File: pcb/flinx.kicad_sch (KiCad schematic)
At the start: 139 parts, among them J1 USB_C_Receptacle_USB2.0_14P, SW1 SW_Push, SW10 SW_Push, SW11 SW_Push, SW12 SW_Push, SW13 SW_Push, SW14 SW_Push, SW15 SW_Push, SW16 SW_Push, SW17 SW_Push, SW18 SW_Push, SW19 SW_Push, SW2 SW_Push, SW20 SW_Push, SW21 SW_Push, SW22 SW_Push, SW23 SW_Push, SW24 SW_Push, SW25 SW_Push, SW26 SW_Push, SW27 SW_Push, SW28 SW_Push, SW29 SW_Push, SW3 SW_Push, SW30 SW_Push, SW31 SW_Push, SW32 SW_Push, SW33 SW_Push, SW34 SW_Push, SW35 SW_Push, SW36 SW_Push, SW37 SW_Push, SW38 SW_Push, SW39 SW_Push, SW4 SW_Push, SW40 SW_Push, SW41 SW_Push, SW42 SW_Push, SW43 SW_Push, SW44 SW_Push, SW45 SW_Push, SW46 SW_Push, SW47 SW_Push, SW48 SW_Push, SW49 SW_SPDT, SW5 SW_Push, SW6 SW_Push, SW7 SW_Push, SW8 SW_Push, SW9 SW_Push, U1 nRF52833_QDxx, U2 TP4057, Y1 32MHz

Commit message: Update PCB
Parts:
- removed Y1: 32MHz, Crystal:Crystal_SMD_MicroCrystal_CC7V-T1A-2Pin_3.2x1.5mm, symbol Device:Crystal
- added Y1: 32MHz, Crystal:Crystal_SMD_SeikoEpson_FA128-4Pin_2.0x1.6mm, symbol Device:Crystal_GND24
- L1, L3, L4: value 4.7nH -> 4.7 nH
- L2: value 2.2nH -> 2.2 nH
- L5: value 2.7nH -> 2.7 nH
- L6: value 3.3nH -> 3.3 nH
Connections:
- net GND: now also Y1.2 (G), Y1.4 (G)
- net at C1.1, U1.28 (XC1): now also Y1.1
- net at C2.1, U1.29 (XC2): now also Y1.3
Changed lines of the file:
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@@
 	)
 	(junction
-		(at 130.81 87.63)
+		(at 31.75 78.74)
 		(diameter 0)
 		(color 0 0 0 0)
 	)
 	(junction
-		(at 31.75 78.74)
+		(at 123.19 87.63)
 		(diameter 0)
 		(color 0 0 0 0)
@@
 	)
 	(junction
+		(at 130.81 87.63)
+		(diameter 0)
+		(color 0 0 0 0)
+	)
+	(junction
 		(at 207.01 163.83)
 		(diameter 0)
@@
 	)
 	(junction
-		(at 123.19 87.63)
-		(diameter 0)
-		(color 0 0 0 0)
-	)
-	(junction
 		(at 69.85 163.83)
 		(diameter 0)
@@
 	(wire
 		(pts
+			(xy 127 92.71) (xy 127 95.25)
+		)
+		(stroke
+			(width 0)
+			(type default)
+		)
+	)
+	(wire
+		(pts
 			(xy 38.1 43.18) (xy 38.1 48.26)
 		)
@@
 			)
 		)
-		(property "Value" "4.7nH"
+		(property "Value" "4.7 nH"
 			(at 43.18 40.64 90)
 			(show_name no)
@@
 			)
 		)
-		(property "Value" "4.7nH"
+		(property "Value" "4.7 nH"
 			(at 85.09 85.09 90)
 			(show_name no)
@@
 			)
 		)
-		(property "Value" "2.7nH"
+		(property "Value" "2.7 nH"
 			(at 102.87 105.4099 0)
 			(show_name no)
@@
 			)
 		)
-		(property "Value" "4.7nH"
+		(property "Value" "4.7 nH"
 			(at 52.07 40.64 90)
 			(show_name no)
@@
 			)
 		)
-		(property "Value" "3.3nH"
+		(property "Value" "3.3 nH"
 			(at 106.68 97.79 90)
 			(show_name no)
@@
 			)
 		)
-		(property "Value" "2.2nH"
+		(property "Value" "2.2 nH"
 			(at 92.71 85.09 90)
 			(show_name no)
@@
 	)
 	(symbol
+		(lib_id "Device:Crystal_GND24")
+		(at 127 87.63 0)
+		(unit 1)
+		(body_style 1)
+		(exclude_from_sim no)
+		(in_bom yes)
+		(on_board yes)
+		(in_pos_files yes)
+		(dnp no)
+		(fields_autoplaced yes)
+		(property "Reference" "Y1"
+			(at 127 78.74 0)
+			(show_name no)
+			(do_not_autoplace no)
+			(effects
+				(font
+					(size 1.27 1.27)
+				)
+			)
+		)
+		(property "Value" "32MHz"
+			(at 127 81.28 0)
+			(show_name no)
+			(do_not_autoplace no)
+			(effects
+				(font
+					(size 1.27 1.27)
+				)
+			)
+		)
+		(property "Footprint" "Crystal:Crystal_SMD_SeikoEpson_FA128-4Pin_2.0x1.6mm"
+			(at 127 87.63 0)
+			(hide yes)
+			(show_name no)
+			(do_not_autoplace no)
+			(effects
+				(font
+					(size 1.27 1.27)
+				)
+			)
+		)
+		(property "Datasheet" ""
+			(at 127 87.63 0)
+			(hide yes)
+			(show_name no)
+			(do_not_autoplace no)
+			(effects
+				(font
+					(size 1.27 1.27)
+				)
+			)
+		)
+		(property "Description" "Four pin crystal, GND on pins 2 and 4"
+			(at 127 87.63 0)
+			(hide yes)
+			(show_name no)
+			(do_not_autoplace no)
+			(effects
+				(font
+					(size 1.27 1.27)
+				)
+			)
+		)
+		(property private "KLC_S3.3" "The rectangle is not a symbol body but a graphical element"
+			(at 127 100.33 0)
+			(hide yes)
+			(show_name yes)
+			(do_not_autoplace no)
+			(effects
+				(font
+					(size 1.27 1.27)
+				)
+			)
+		)
+		(property private "KLC_S4.1" "Some pins are on 50mil grid to make the symbol small"
+			(at 127 102.87 0)
+			(hide yes)
+			(show_name yes)
+			(do_not_autoplace no)
+			(effects
+				(font
+					(size 1.27 1.27)
+				)
+			)
+		)
+		(pin "3"
+		)
+		(pin "4"
+		)
+		(pin "1"
+		)
+		(pin "2"
+		)
+		(instances
+			(project "flinx"
+				(path "/cb115450-b63d-4583-9c68-cd7130599f33"
+					(reference "Y1")
+					(unit 1)
+				)
+			)
+		)
+	)
+	(symbol
 		(lib_id "Device:R")
 		(at 267.97 104.14 0)
@@
 					(unit 1)
 				)
-			)
-		)
-	)
-	(symbol
-		(lib_id "Device:Crystal")
-		(at 127 87.63 0)
-		(unit 1)
-		(body_style 1)
-		(exclude_from_sim no)
-		(in_bom yes)
-		(on_board yes)
-		(in_pos_files yes)
-		(dnp no)
-		(fields_autoplaced yes)
-		(property "Reference" "Y1"
-			(at 127 80.01 0)
-			(show_name no)
-			(do_not_autoplace no)
-			(effects
-				(font
-					(size 1.27 1.27)
-				)
-			)
-		)
-		(property "Value" "32MHz"
-			(at 127 82.55 0)
-			(show_name no)
-			(do_not_autoplace no)
-			(effects
-				(font
-					(size 1.27 1.27)
-				)
-			)
-		)
-		(property "Footprint" "Crystal:Crystal_SMD_MicroCrystal_CC7V-T1A-2Pin_3.2x1.5mm"
-			(at 127 87.63 0)
-			(hide yes)
-			(show_name no)
-			(do_not_autoplace no)
-			(effects
-				(font
-					(size 1.27 1.27)
-				)
-			)
-		)
-		(property "Datasheet" ""
-			(at 127 87.63 0)
-			(hide yes)
-			(show_name no)
-			(do_not_autoplace no)
-			(effects
-				(font
-					(size 1.27 1.27)
-				)
-			)
-		)
-		(property "Description" "Two pin crystal"
-			(at 127 87.63 0)
-			(hide yes)
-			(show_name no)
-			(do_not_autoplace no)
-			(effects
-				(font
-					(size 1.27 1.27)
-				)
-			)
-		)
-		(pin "1"
-		)
-		(pin "2"
-		)
-		(instances
-			(project "flinx"
-				(path "/cb115450-b63d-4583-9c68-cd7130599f33"
-					(reference "Y1")
-					(unit 1)
-				)

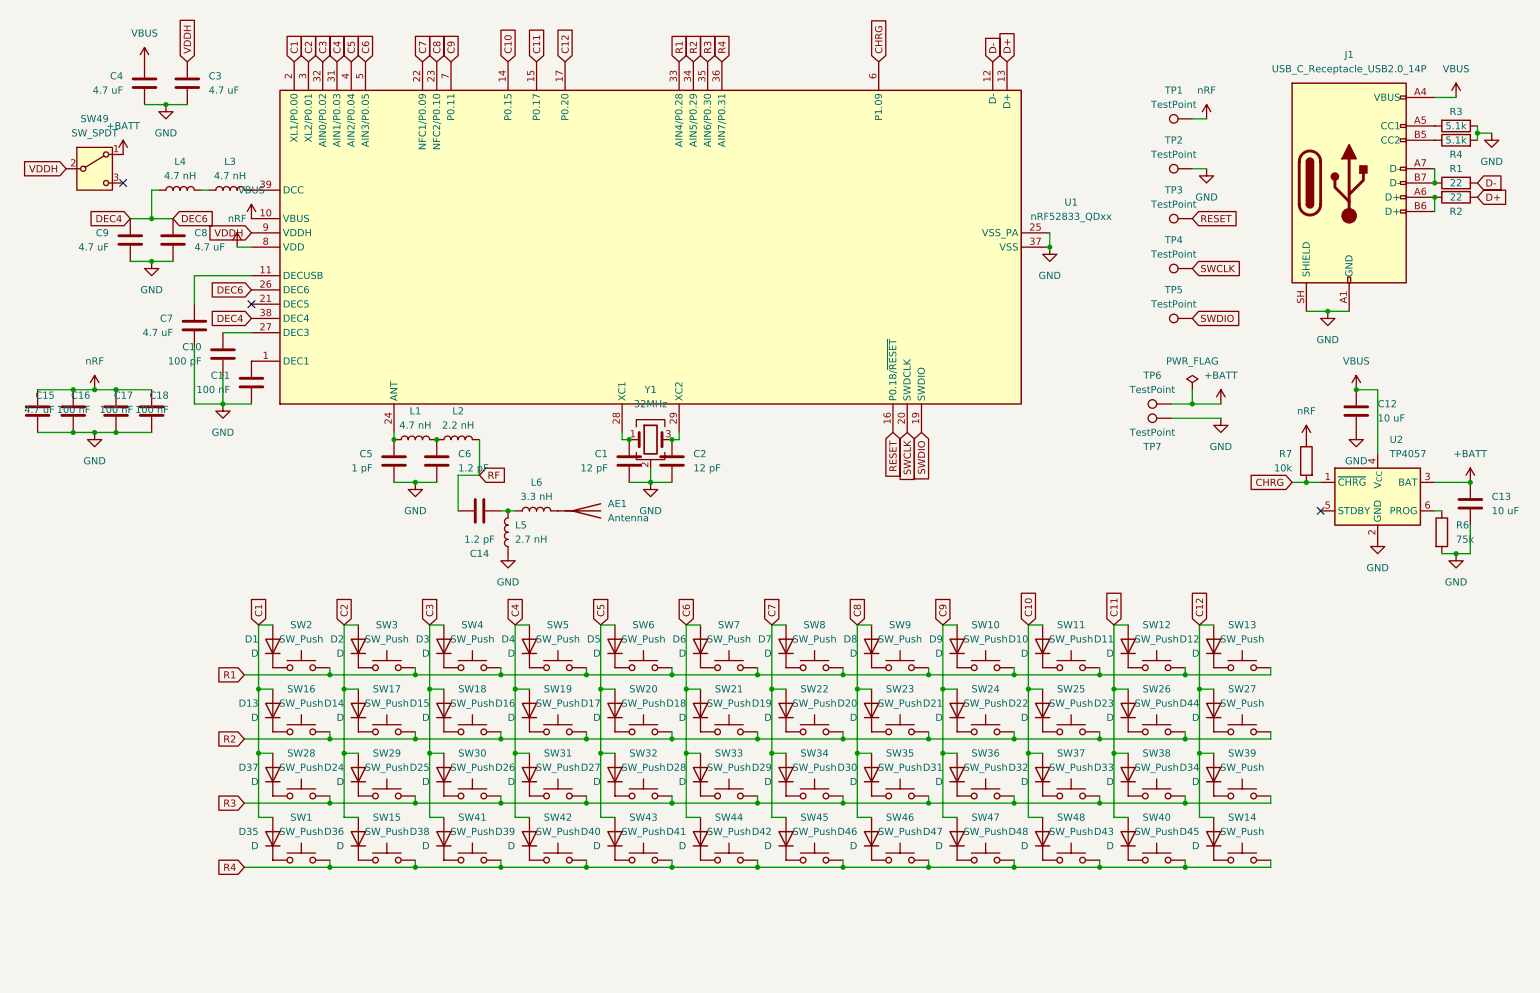
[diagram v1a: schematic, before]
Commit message: Swap to BL654
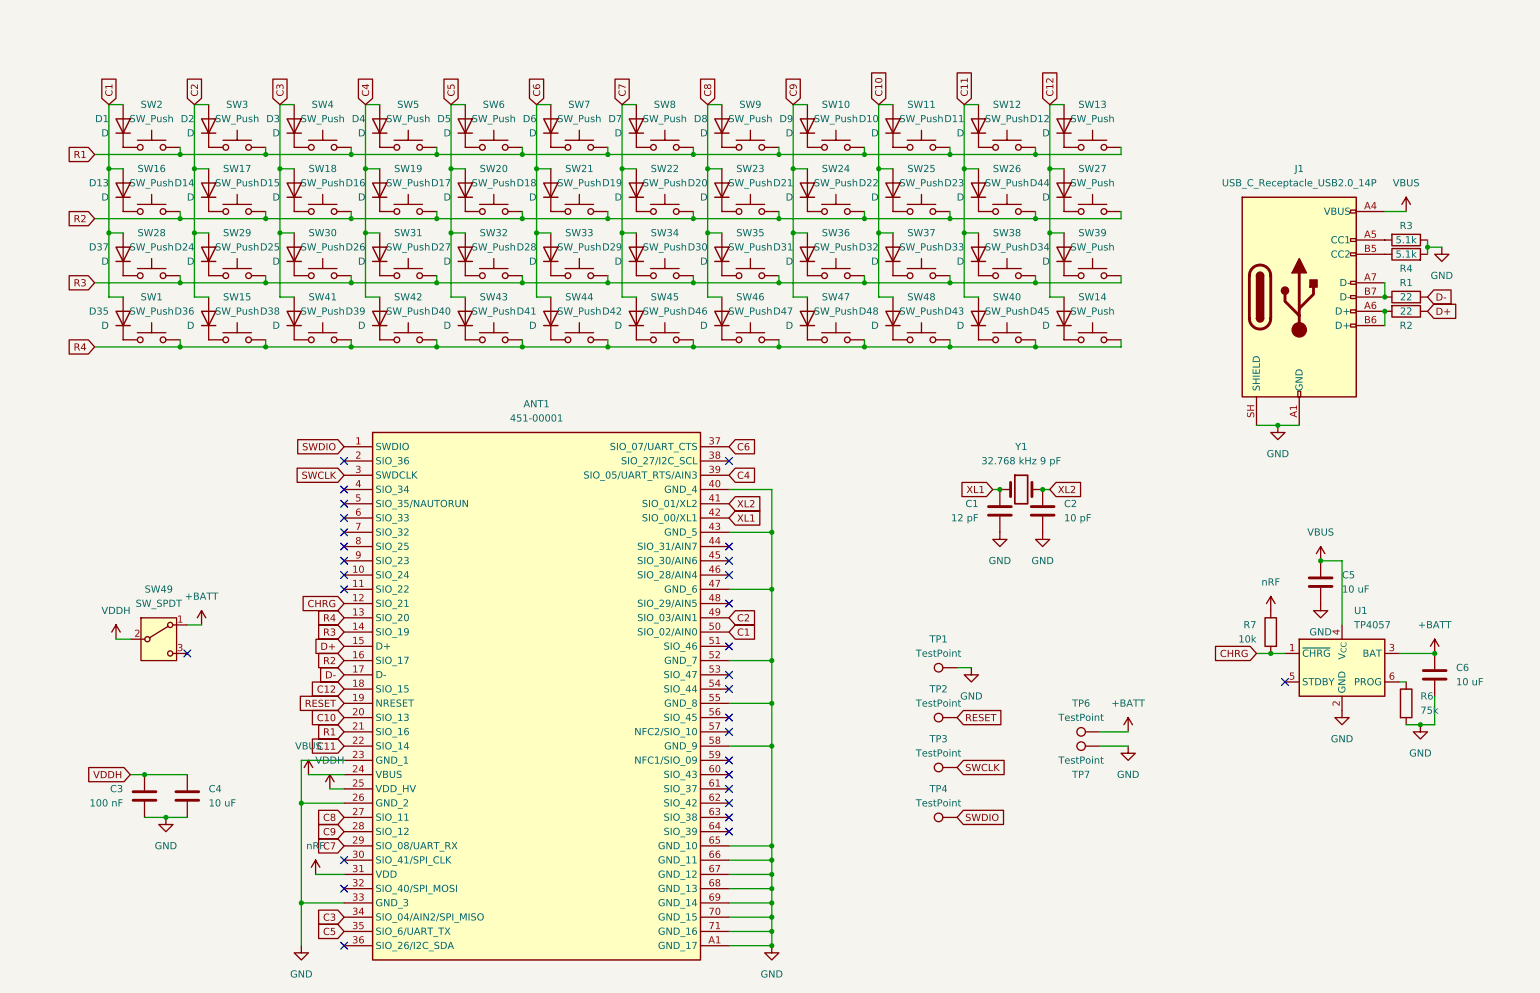
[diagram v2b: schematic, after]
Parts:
- removed AE1: Antenna, RF_Antenna:Johanson_2450AT18x100, symbol Device:Antenna
- removed C10: 100 pF, Capacitor_SMD:C_0603_1608Metric, symbol Device:C
- removed C11, C16, C17, C18: 100 nF, Capacitor_SMD:C_0603_1608Metric, symbol Device:C
- removed C14, C6: 1.2 pF, Capacitor_SMD:C_0603_1608Metric, symbol Device:C
- removed C15, C7, C8, C9: 4.7 uF, Capacitor_SMD:C_0603_1608Metric, symbol Device:C
- removed C5: 1 pF, Capacitor_SMD:C_0603_1608Metric, symbol Device:C
- removed L1, L3, L4: 4.7 nH, Inductor_SMD:L_0603_1608Metric, symbol Device:L
- removed L2: 2.2 nH, Inductor_SMD:L_0603_1608Metric, symbol Device:L
- removed L5: 2.7 nH, Inductor_SMD:L_0603_1608Metric, symbol Device:L
- removed L6: 3.3 nH, Inductor_SMD:L_0603_1608Metric, symbol Device:L
- removed TP5: TestPoint, Project:Pad_SMD_1.5x1.5, symbol Connector:TestPoint
- removed U1: nRF52833_QDxx, Package_DFN_QFN:QFN-40-1EP_5x5mm_P0.4mm_EP3.6x3.6mm, symbol MCU_Nordic:nRF52833_QDxx
- removed Y1: 32MHz, Crystal:Crystal_SMD_SeikoEpson_FA128-4Pin_2.0x1.6mm, symbol Device:Crystal_GND24
- added ANT1: 451-00001, Project:45100001, symbol Project:451-00001
- added Y1: 32.768 kHz 9 pF, Crystal:Crystal_SMD_MicroCrystal_CC7V-T1A-2Pin_3.2x1.5mm_HandSoldering, symbol Device:Crystal
- C2: value 12 pF -> 10 pF
- C3: value 4.7 uF -> 100 nF
- C4: value 4.7 uF -> 10 uF
- renumbered C12 to C5, C13 to C6, U2 to U1
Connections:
- net C1: now also ANT1.50 (SIO_02/AIN0)
- net C10: now also ANT1.20 (SIO_13)
- net C11: now also ANT1.22 (SIO_14)
- net C12: now also ANT1.18 (SIO_15)
- net C2: now also ANT1.49 (SIO_03/AIN1)
- net C3: now also ANT1.34 (SIO_04/AIN2/SPI_MISO)
- net C4: now also ANT1.39 (SIO_05/UART_RTS/AIN3)
- net C5: now also ANT1.35 (SIO_6/UART_TX)
- net C6: now also ANT1.37 (SIO_07/UART_CTS)
- net C7: now also ANT1.29 (SIO_08/UART_RX)
- net C8: now also ANT1.27 (SIO_11)
- net C9: now also ANT1.28 (SIO_12)
- net CHRG: now also ANT1.12 (SIO_21)
- net D+: now also ANT1.15 (D+)
- net D-: now also ANT1.17 (D-)
- net GND: now also TP1.1, ANT1.23 (GND_1), ANT1.26 (GND_2), ANT1.33 (GND_3), ANT1.40 (GND_4), ANT1.43 (GND_5), ANT1.47 (GND_6), ANT1.52 (GND_7), ANT1.55 (GND_8), ANT1.58 (GND_9), ANT1.65 (GND_10), ANT1.66 (GND_11), ANT1.67 (GND_12), ANT1.68 (GND_13), ANT1.69 (GND_14), ANT1.70 (GND_15), ANT1.71 (GND_16), ANT1.A1 (GND_17); no longer TP2.1
- net R1: now also ANT1.21 (SIO_16)
- net R2: now also ANT1.16 (SIO_17)
- net R3: now also ANT1.14 (SIO_19)
- net R4: now also ANT1.13 (SIO_20)
- net RESET: now also TP2.1, ANT1.19 (NRESET); no longer TP3.1
- net SWCLK: now also TP3.1, ANT1.3 (SWDCLK); no longer TP4.1
- net SWDIO: now also TP4.1, ANT1.1 (SWDIO)
- net VBUS: now also ANT1.24 (VBUS); no longer C4.1
- net VDDH: now also C4.1, ANT1.25 (VDD_HV)
- net nRF: now also ANT1.31 (VDD); no longer TP1.1
- net XL1: now reaches C1.1
- net XL1: now also ANT1.42 (SIO_00/XL1), Y1.1
- net XL2: now reaches C2.1
- net XL2: now also ANT1.41 (SIO_01/XL2), Y1.2
- no-connect marks 3 -> 30
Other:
- moved on the sheet: C5, C6, D1, D10, D11, D12, D13, D14, D15, D16, D17, D18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

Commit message: Move decoupling caps
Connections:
- net GND: now also C3.1, C4.1; no longer C3.2, C4.2
- net VDDH: now also C3.2, C4.2; no longer C3.1, C4.1
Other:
- moved on the sheet: C4
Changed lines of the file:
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@@
 	)
 	(junction
-		(at 148.59 114.3)
+		(at 36.83 147.32)
 		(diameter 0)
 		(color 0 0 0 0)
 	)
 	(junction
-		(at 195.58 36.83)
+		(at 148.59 114.3)
 		(diameter 0)
 		(color 0 0 0 0)
 	)
 	(junction
-		(at 119.38 48.26)
+		(at 195.58 36.83)
 		(diameter 0)
 		(color 0 0 0 0)
 	)
 	(junction
-		(at 36.83 147.32)
+		(at 119.38 48.26)
 		(diameter 0)
 		(color 0 0 0 0)
@@
 	(wire
 		(pts
-			(xy 34.29 147.32) (xy 36.83 147.32)
-		)
-		(stroke
-			(width 0)
-			(type default)
-		)
-	)
-	(wire
-		(pts
 			(xy 265.43 53.34) (xy 267.97 53.34)
 		)
@@
 	(wire
 		(pts
+			(xy 36.83 147.32) (xy 44.45 147.32)
+		)
+		(stroke
+			(width 0)
+			(type default)
+		)
+	)
+	(wire
+		(pts
 			(xy 58.42 36.83) (xy 73.66 36.83)
 		)
@@
 	(wire
 		(pts
-			(xy 36.83 147.32) (xy 44.45 147.32)
+			(xy 58.42 59.69) (xy 73.66 59.69)
 		)
 		(stroke
@@
 	(wire
 		(pts
-			(xy 58.42 59.69) (xy 73.66 59.69)
+			(xy 60.96 50.8) (xy 60.96 62.23)
 		)
 		(stroke
@@
 	(wire
 		(pts
-			(xy 60.96 50.8) (xy 60.96 62.23)
+			(xy 88.9 71.12) (xy 88.9 69.85)
 		)
 		(stroke
@@
 	(wire
 		(pts
-			(xy 88.9 71.12) (xy 88.9 69.85)
+			(xy 187.96 96.52) (xy 189.23 96.52)
 		)
 		(stroke
@@
 	(wire
 		(pts
-			(xy 187.96 96.52) (xy 189.23 96.52)
+			(xy 34.29 147.32) (xy 36.83 147.32)
 		)
 		(stroke
@@
 	(symbol
 		(lib_id "Device:C")
-		(at 44.45 151.13 0)
+		(at 44.45 151.13 180)
 		(unit 1)
 		(body_style 1)
@@
 					(size 1.27 1.27)
 				)
-				(justify left)
+				(justify right)
 			)
 		)
@@
 					(size 1.27 1.27)
 				)
-				(justify left)
+				(justify right)
 			)
 		)
 		(property "Footprint" "Capacitor_SMD:C_0603_1608Metric"
-			(at 45.4152 154.94 0)
+			(at 43.4848 147.32 0)
 			(hide yes)
 			(show_name no)
@@
 	)
 	(symbol
-		(lib_id "Device:C")
-		(at 36.83 151.13 0)
-		(mirror y)
-		(unit 1)
-		(body_style 1)
-		(exclude_from_sim no)
-		(in_bom yes)
-		(on_board yes)
-		(in_pos_files yes)
-		(dnp no)
-		(property "Reference" "C3"
-			(at 33.02 149.8599 0)
-			(show_name no)
-			(do_not_autoplace no)
-			(effects
-				(font
-					(size 1.27 1.27)
-				)
-				(justify left)
-			)
-		)
-		(property "Value" "100 nF"
-			(at 33.02 152.3999 0)
-			(show_name no)
-			(do_not_autoplace no)
-			(effects
-				(font
-					(size 1.27 1.27)
-				)
-				(justify left)
-			)
-		)
-		(property "Footprint" "Capacitor_SMD:C_0603_1608Metric"
-			(at 35.8648 154.94 0)
-			(hide yes)
-			(show_name no)
-			(do_not_autoplace no)
-			(effects
-				(font
-					(size 1.27 1.27)
-				)
-			)
-		)
-		(property "Datasheet" ""
-			(at 36.83 151.13 0)
-			(hide yes)
-			(show_name no)
-			(do_not_autoplace no)
-			(effects
-				(font
-					(size 1.27 1.27)
-				)
-			)
-		)
-		(property "Description" "Unpolarized capacitor"
-			(at 36.83 151.13 0)
-			(hide yes)
-			(show_name no)
-			(do_not_autoplace no)
-			(effects
-				(font
-					(size 1.27 1.27)
-				)
-			)
-		)
-		(pin "1"
-		)
-		(pin "2"
-		)
-		(instances
-			(project "flinx"
-				(path "/cb115450-b63d-4583-9c68-cd7130599f33"
-					(reference "C3")
-					(unit 1)
-				)
-			)
-		)
-	)
-	(symbol
 		(lib_id "Device:D")
 		(at 124.46 54.61 270)
@@
 					(unit 1)
 				)
+			)
+		)
+	)
+	(symbol
+		(lib_id "Device:C")
+		(at 36.83 151.13 0)
+		(mirror x)
+		(unit 1)
+		(body_style 1)
+		(exclude_from_sim no)
+		(in_bom yes)
+		(on_board yes)
+		(in_pos_files yes)
+		(dnp no)
+		(property "Reference" "C3"
+			(at 33.02 149.8599 0)
+			(show_name no)
+			(do_not_autoplace no)
+			(effects
+				(font
+					(size 1.27 1.27)
+				)
+				(justify right)
+			)
+		)
+		(property "Value" "100 nF"
+			(at 33.02 152.3999 0)
+			(show_name no)
+			(do_not_autoplace no)
+			(effects
+				(font
+					(size 1.27 1.27)
+				)
+				(justify right)
+			)
+		)
+		(property "Footprint" "Capacitor_SMD:C_0603_1608Metric"
+			(at 37.7952 147.32 0)
+			(hide yes)
+			(show_name no)
+			(do_not_autoplace no)
+			(effects
+				(font
+					(size 1.27 1.27)
+				)
+			)
+		)
+		(property "Datasheet" ""
+			(at 36.83 151.13 0)
+			(hide yes)
+			(show_name no)
+			(do_not_autoplace no)
+			(effects
+				(font
+					(size 1.27 1.27)
+				)
+			)
+		)
+		(property "Description" "Unpolarized capacitor"
+			(at 36.83 151.13 0)
+			(hide yes)
+			(show_name no)
+			(do_not_autoplace no)
+			(effects
+				(font
+					(size 1.27 1.27)
+				)
+			)
+		)
+		(pin "1"
+		)
+		(pin "2"
+		)
+		(instances
+			(project "flinx"
+				(path "/cb115450-b63d-4583-9c68-cd7130599f33"
+					(reference "C3")
+					(unit 1)
+				)

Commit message: Update value
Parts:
- R6: value 75k -> 10k
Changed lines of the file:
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@@
 	)
 	(junction
-		(at 119.38 71.12)
+		(at 40.64 147.32)
 		(diameter 0)
 		(color 0 0 0 0)
 	)
 	(junction
-		(at 36.83 147.32)
+		(at 119.38 71.12)
 		(diameter 0)
 		(color 0 0 0 0)
@@
 	(wire
 		(pts
+			(xy 40.64 147.32) (xy 44.45 147.32)
+		)
+		(stroke
+			(width 0)
+			(type default)
+		)
+	)
+	(wire
+		(pts
 			(xy 237.49 125.73) (xy 240.03 125.73)
 		)
@@
 	(wire
 		(pts
-			(xy 36.83 147.32) (xy 44.45 147.32)
+			(xy 36.83 147.32) (xy 40.64 147.32)
 		)
 		(stroke
@@
 	(wire
 		(pts
-			(xy 34.29 147.32) (xy 36.83 147.32)
-		)
-		(stroke
-			(width 0)
-			(type default)
-		)
-	)
-	(wire
-		(pts
 			(xy 210.82 71.12) (xy 210.82 69.85)
 		)
@@
 		)
 	)
-	(global_label "VDDH"
-		(shape input)
-		(at 34.29 147.32 180)
-		(fields_autoplaced yes)
-		(effects
-			(font
-				(size 1.27 1.27)
-			)
-			(justify right)
-		)
-		(property "Intersheetrefs" "${INTERSHEET_REFS}"
-			(at 26.3457 147.32 0)
-			(hide yes)
-			(show_name no)
-			(do_not_autoplace no)
-			(effects
-				(font
-					(size 1.27 1.27)
-				)
-				(justify right)
-			)
-		)
-	)
 	(global_label "R1"
 		(shape input)
@@
 			)
 		)
-		(property "Value" "75k"
+		(property "Value" "10k"
 			(at 264.16 135.8899 0)
 			(show_name no)
@@
 					(unit 1)
 				)
+			)
+		)
+	)
+	(symbol
+		(lib_id "power:+BATT")
+		(at 40.64 147.32 0)
+		(unit 1)
+		(body_style 1)
+		(exclude_from_sim no)
+		(in_bom yes)
+		(on_board yes)
+		(in_pos_files yes)
+		(dnp no)
+		(fields_autoplaced yes)
+		(property "Reference" "#PWR021"
+			(at 40.64 151.13 0)
+			(hide yes)
+			(show_name no)
+			(do_not_autoplace no)
+			(effects
+				(font
+					(size 1.27 1.27)
+				)
+			)
+		)
+		(property "Value" "VDDH"
+			(at 40.64 142.24 0)
+			(show_name no)
+			(do_not_autoplace no)
+			(effects
+				(font
+					(size 1.27 1.27)
+				)
+			)
+		)
+		(property "Footprint" ""
+			(at 40.64 147.32 0)
+			(hide yes)
+			(show_name no)
+			(do_not_autoplace no)
+			(effects
+				(font
+					(size 1.27 1.27)
+				)
+			)
+		)
+		(property "Datasheet" ""
+			(at 40.64 147.32 0)
+			(hide yes)
+			(show_name no)
+			(do_not_autoplace no)
+			(effects
+				(font
+					(size 1.27 1.27)
+				)
+			)
+		)
+		(property "Description" "Power symbol creates a global label with name \"+BATT\""
+			(at 40.64 147.32 0)
+			(hide yes)
+			(show_name no)
+			(do_not_autoplace no)
+			(effects
+				(font
+					(size 1.27 1.27)
+				)
+			)
+		)
+		(pin "1"
+		)
+		(instances
+			(project "flinx"
+				(path "/cb115450-b63d-4583-9c68-cd7130599f33"
+					(reference "#PWR021")
+					(unit 1)
+				)
